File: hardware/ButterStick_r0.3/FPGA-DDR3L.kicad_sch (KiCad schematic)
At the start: 1 part, among them U2 ECP5UM5G_85_CABGA381

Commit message: hw.r0_3: major blocks roughly routed
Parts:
- renumbered U2 to U4
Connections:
- net 1v35: no longer U4.L14 (VCCIO3[3]), U4.L15 (VCCIO3[3]), U4.M15 (VCCIO3[3]), U4.M18 (PR50D/RDQ53), U4.M19 (PR47D/PCLKC3_0/RDQ53), U4.N19 (PR83A/RDQ89), U4.T20 (PR86C/RDQ89), U4.U16 (PR92C/LRC_GPLL0T_IN/RDQ89)
- net A0: no longer U4.U17 (PR92B/RDQ89)
- net A1: now also U4.H18 (PR20A/RDQ17); no longer U4.H20 (PR41B/RDQSN41)
- net A10: now also U4.J18 (PR41C/GR_PCLK2_0/RDQ41); no longer U4.K20 (PR44D/PCLKC2_0/RDQ41)
- net A15: now also U4.J16 (PR20D/RDQ17); no longer U4.K19 (PR44B/PCLKC2_1/RDQ41)
- net A5: no longer U4.T17 (PR92D/LRC_GPLL0C_IN/RDQ89)
- net A7: now also U4.H17 (PR20B/RDQ17); no longer U4.J19 (PR44A/PCLKT2_1/RDQ41)
- net BA1: no longer U4.M20 (PR47B/PCLKC3_1/RDQ53)
- net CK1_N: now also U4.K19 (PR44B/PCLKC2_1/RDQ41)
- net CK1_P: now also U4.J19 (PR44A/PCLKT2_1/RDQ41)
- net CKE1: now also U4.K20 (PR44D/PCLKC2_0/RDQ41); no longer U4.J16 (PR20D/RDQ17)
- net CS1: now also U4.H20 (PR41B/RDQSN41); no longer U4.H16 (PR17D/RDQ17)
- net DQ0: no longer U4.U19 (PR89C/RDQ89)
- net DQ1: no longer U4.T18 (PR89D/RDQ89)
- net DQ10: no longer U4.L16 (PR50A/GR_PCLK3_0/RDQ53)
- net DQ11: no longer U4.R16 (PR56C/RDQ53)
- net DQ12: no longer U4.N18 (PR53C/RDQ53)
- net DQ13: no longer U4.R17 (PR56D/RDQ53)
- net DQ14: no longer U4.N17 (PR56A/RDQ53)
- net DQ15: no longer U4.P17 (PR53D/RDQ53)
- net DQ2: no longer U4.U18 (PR92A/RDQ89)
- net DQ3: no longer U4.R20 (PR86B/RDQ89)
- net DQ4: no longer U4.P18 (PR83D/RDQ89)
- net DQ5: no longer U4.P20 (PR86A/RDQ89)
- net DQ6: no longer U4.P19 (PR83C/RDQ89)
- net DQ7: no longer U4.N20 (PR83B/RDQ89)
- net DQ8: no longer U4.L19 (PR47C/PCLKT3_0/RDQ53)
- net DQ9: no longer U4.L17 (PR50B/RDQ53)
- net LDM: no longer U4.U20 (PR86D/RDQ89)
- net LDQS_N: no longer U4.R18 (PR89B/RDQSN89)
- net LDQS_P: no longer U4.T19 (PR89A/RDQS89)
- net UDM: no longer U4.L18 (PR50C/GR_PCLK3_1/RDQ53)
- net UDQS_N: no longer U4.M17 (PR53B/RDQSN53)
- net UDQS_P: no longer U4.N16 (PR53A/RDQS53)
- net VREF: no longer U4.P16 (PR56B/VREF1_3/RDQ53)
- new net: U4.L14 (VCCIO3[3]), U4.L15 (VCCIO3[3]), U4.M15 (VCCIO3[3])
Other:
- moved on the sheet: U4E
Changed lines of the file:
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@@
   (page 8 19)
   (paper "A4")
-  (no_connect (at 90.17 97.79))
   (no_connect (at 176.53 95.25))
   (no_connect (at 90.17 95.25))
-  (wire (pts (xy 59.69 80.01) (xy 78.74 80.01)))
-  (wire (pts (xy 66.04 95.25) (xy 73.66 95.25)))
-  (wire (pts (xy 66.04 97.79) (xy 73.66 97.79)))
+  (no_connect (at 90.17 97.79))
+  (wire (pts (xy 59.69 124.46) (xy 78.74 124.46)))
   (wire (pts (xy 82.55 54.61) (xy 90.17 54.61)))
   (wire (pts (xy 82.55 57.15) (xy 90.17 57.15)))
@@
   (wire (pts (xy 82.55 74.93) (xy 90.17 74.93)))
   (wire (pts (xy 82.55 77.47) (xy 90.17 77.47)))
-  (wire (pts (xy 82.55 82.55) (xy 90.17 82.55)))
+  (wire (pts (xy 82.55 85.09) (xy 90.17 85.09)))
+  (wire (pts (xy 82.55 87.63) (xy 90.17 87.63)))
   (wire (pts (xy 82.55 90.17) (xy 90.17 90.17)))
   (wire (pts (xy 82.55 92.71) (xy 90.17 92.71)))
@@
   (wire (pts (xy 82.55 120.65) (xy 90.17 120.65)))
   (wire (pts (xy 82.55 123.19) (xy 90.17 123.19)))
+  (wire (pts (xy 82.55 125.73) (xy 90.17 125.73)))
   (wire (pts (xy 82.55 128.27) (xy 90.17 128.27)))
   (wire (pts (xy 82.55 130.81) (xy 90.17 130.81)))
@@
     (effects (font (size 0.508 0.508)) (justify left bottom))
   )
-  (label "A2" (at 59.69 80.01 0)
-    (effects (font (size 1.27 1.27)) (justify left bottom))
-  )
-  (label "CK1_P" (at 66.04 95.25 0)
-    (effects (font (size 1.27 1.27)) (justify left bottom))
-  )
-  (label "CK1_N" (at 66.04 97.79 0)
+  (label "A2" (at 59.69 124.46 0)
     (effects (font (size 1.27 1.27)) (justify left bottom))
   )
@@
     (effects (font (size 1.27 1.27)) (justify left bottom))
   )
-  (label "CS1" (at 82.55 82.55 0)
+  (label "A1" (at 82.55 85.09 0)
+    (effects (font (size 1.27 1.27)) (justify left bottom))
+  )
+  (label "A7" (at 82.55 87.63 0)
     (effects (font (size 1.27 1.27)) (justify left bottom))
   )
@@
     (effects (font (size 1.27 1.27)) (justify left bottom))
   )
-  (label "CKE1" (at 82.55 92.71 0)
+  (label "A15" (at 82.55 92.71 0)
     (effects (font (size 1.27 1.27)) (justify left bottom))
   )
@@
     (effects (font (size 1.27 1.27)) (justify left bottom))
   )
-  (label "A1" (at 82.55 123.19 0)
+  (label "CS1" (at 82.55 123.19 0)
+    (effects (font (size 1.27 1.27)) (justify left bottom))
+  )
+  (label "A10" (at 82.55 125.73 0)
     (effects (font (size 1.27 1.27)) (justify left bottom))
   )
@@
     (effects (font (size 1.27 1.27)) (justify left bottom))
   )
-  (label "A7" (at 82.55 130.81 0)
-    (effects (font (size 1.27 1.27)) (justify left bottom))
-  )
-  (label "A15" (at 82.55 133.35 0)
+  (label "CK1_P" (at 82.55 130.81 0)
+    (effects (font (size 1.27 1.27)) (justify left bottom))
+  )
+  (label "CK1_N" (at 82.55 133.35 0)
     (effects (font (size 1.27 1.27)) (justify left bottom))
   )
@@
     (effects (font (size 1.27 1.27)) (justify left bottom))
   )
-  (label "A10" (at 82.55 138.43 0)
+  (label "CKE1" (at 82.55 138.43 0)
     (effects (font (size 1.27 1.27)) (justify left bottom))
   )
@@
     (effects (font (size 1.27 1.27)) (justify right))
   )
-  (symbol (lib_id "gkl_lattice:ECP5UM5G_85_CABGA381") (at 176.53 54.61 0) (unit 5)
-    (property "Reference" "U2" (id 0) (at 184.15 46.99 0)
+  (symbol (lib_id "gkl_lattice:ECP5UM5G_85_CABGA381") (at 176.53 54.61 0) (mirror x) (unit 5)
+    (property "Reference" "U4" (id 0) (at 184.15 62.23 0)
       (effects (font (size 1.524 1.524)) (justify left))
     )
-    (property "Value" "ECP5UM5G_85_CABGA381" (id 1) (at 182.88 49.53 0)
+    (property "Value" "ECP5UM5G_85_CABGA381" (id 1) (at 182.88 59.69 0)
       (effects (font (size 1.524 1.524)) (justify left))
     )
-    (property "Footprint" "gkl_housings_bga:caBGA_381_17x17" (id 2) (at 180.34 53.34 0)
+    (property "Footprint" "gkl_housings_bga:caBGA_381_17x17" (id 2) (at 180.34 55.88 0)
       (effects (font (size 1.524 1.524)) (justify right) hide)
     )
-    (property "Datasheet" "" (id 3) (at 180.34 58.42 0)
+    (property "Datasheet" "" (id 3) (at 180.34 50.8 0)
       (effects (font (size 1.524 1.524)) (justify right) hide)
     )
-    (property "manf#" "ECP5UM5G_85" (id 4) (at 180.34 55.88 0)
+    (property "manf#" "ECP5UM5G_85" (id 4) (at 180.34 53.34 0)
       (effects (font (size 1.524 1.524)) (justify right) hide)
     )
   )
   (symbol (lib_id "gkl_lattice:ECP5UM5G_85_CABGA381") (at 90.17 54.61 0) (unit 4)
-    (property "Reference" "U2" (id 0) (at 96.52 46.99 0)
+    (property "Reference" "U4" (id 0) (at 96.52 46.99 0)
       (effects (font (size 1.524 1.524)) (justify left))
     )

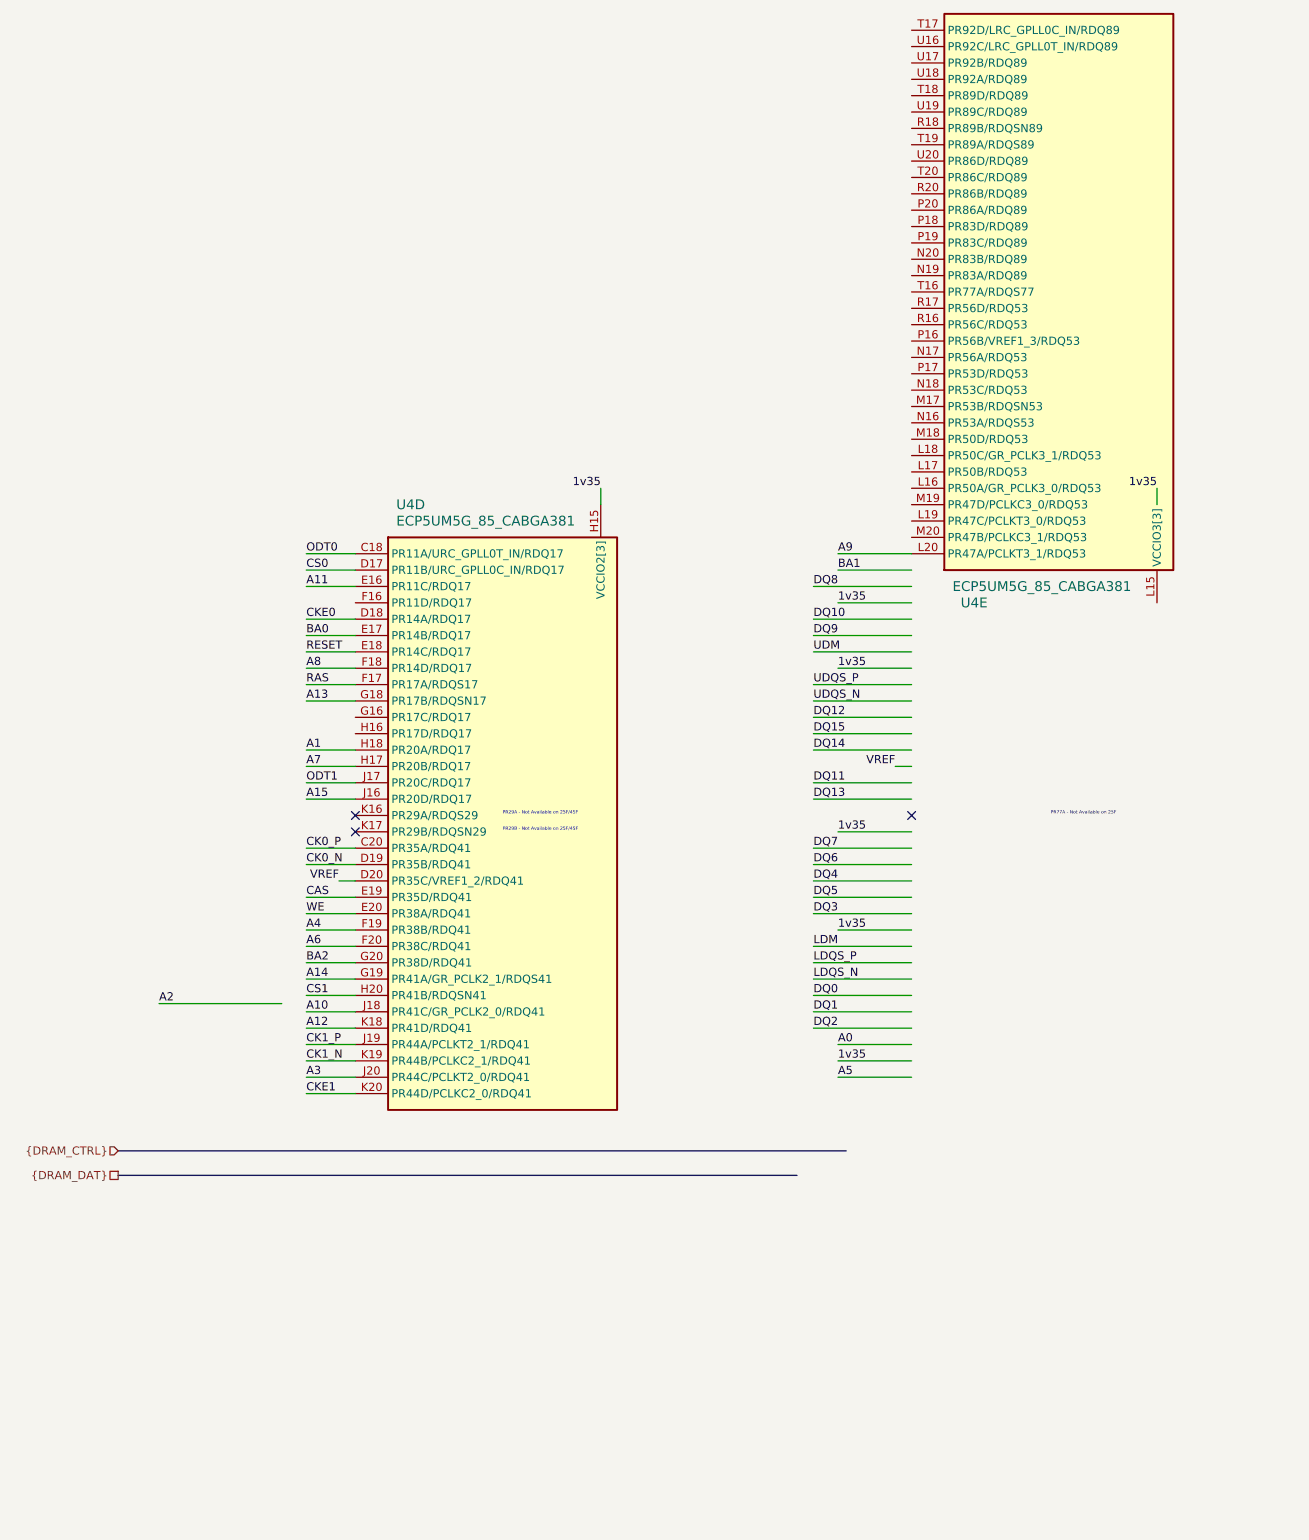
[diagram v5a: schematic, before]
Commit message: hw.r0d3: Length matched all SYZYGY ports
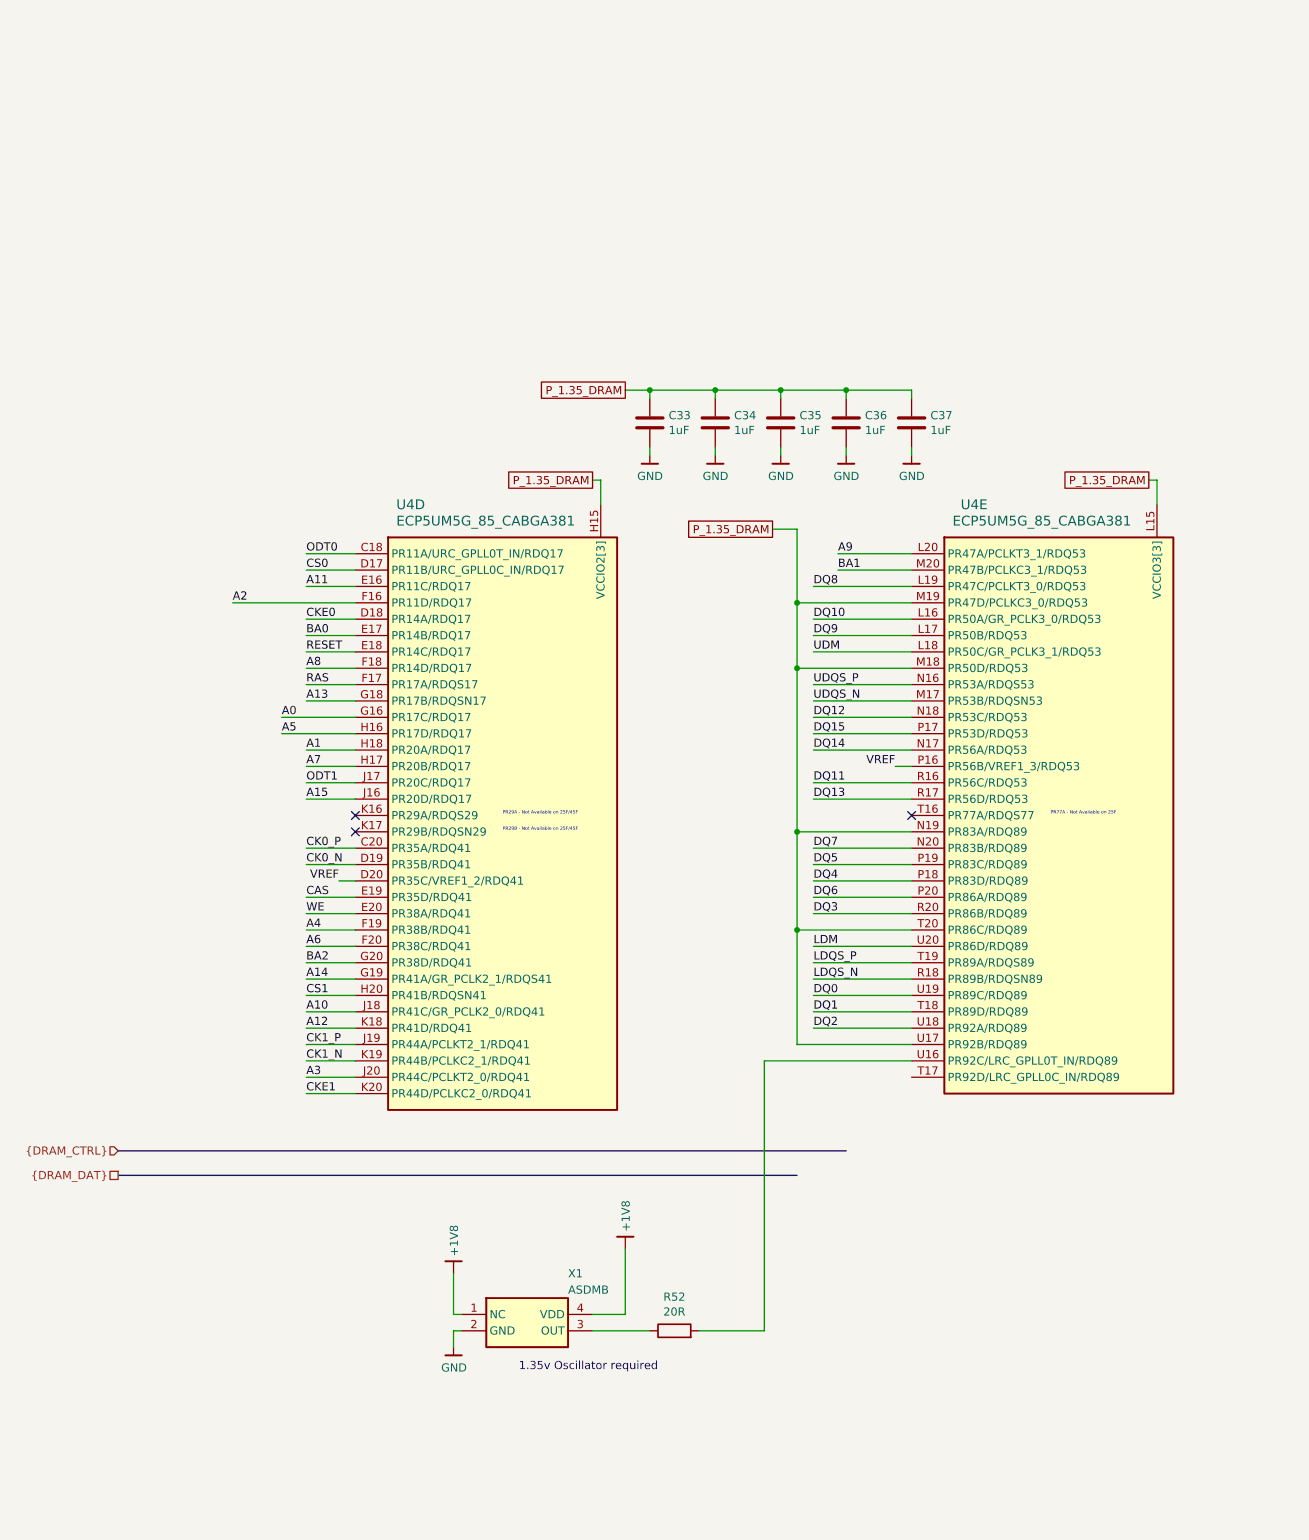
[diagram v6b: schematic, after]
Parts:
- added C33, C34, C35, C36, C37: 1uF, Capacitor_SMD:C_0402_1005Metric, symbol Device:C
- added R52: 20R, Resistor_SMD:R_0402_1005Metric, symbol Device:R
- added X1: ASDMB, gkl_time:Oscilator_2.5x2.0, symbol gkl_time:TYETBCSANF-32.000000
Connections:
- net 1v35 is gone; now on net P_1.35_DRAM: U4.H14 (VCCIO2[3]), U4.H15 (VCCIO2[3]), U4.J15 (VCCIO2[3])
- net A0: now also U4.G16 (PR17C/RDQ17)
- net A2: now also U4.F16 (PR11D/RDQ17)
- net A5: now also U4.H16 (PR17D/RDQ17)
- net BA1: now also U4.M20 (PR47B/PCLKC3_1/RDQ53)
- net DQ0: now also U4.U19 (PR89C/RDQ89)
- net DQ1: now also U4.T18 (PR89D/RDQ89)
- net DQ10: now also U4.L16 (PR50A/GR_PCLK3_0/RDQ53)
- net DQ11: now also U4.R16 (PR56C/RDQ53)
- net DQ12: now also U4.N18 (PR53C/RDQ53)
- net DQ13: now also U4.R17 (PR56D/RDQ53)
- net DQ14: now also U4.N17 (PR56A/RDQ53)
- net DQ15: now also U4.P17 (PR53D/RDQ53)
- net DQ2: now also U4.U18 (PR92A/RDQ89)
- net DQ3: now also U4.R20 (PR86B/RDQ89)
- net DQ4: now also U4.P18 (PR83D/RDQ89)
- net DQ5: now also U4.P19 (PR83C/RDQ89)
- net DQ6: now also U4.P20 (PR86A/RDQ89)
- net DQ7: now also U4.N20 (PR83B/RDQ89)
- net DQ8: now also U4.L19 (PR47C/PCLKT3_0/RDQ53)
- net DQ9: now also U4.L17 (PR50B/RDQ53)
- net LDM: now also U4.U20 (PR86D/RDQ89)
- net LDQS_N: now also U4.R18 (PR89B/RDQSN89)
- net LDQS_P: now also U4.T19 (PR89A/RDQS89)
- net UDM: now also U4.L18 (PR50C/GR_PCLK3_1/RDQ53)
- net UDQS_N: now also U4.M17 (PR53B/RDQSN53)
- net UDQS_P: now also U4.N16 (PR53A/RDQS53)
- net VREF: now also U4.P16 (PR56B/VREF1_3/RDQ53)
- net P_1.35_DRAM: now reaches U4.L14 (VCCIO3[3]), U4.L15 (VCCIO3[3]), U4.M15 (VCCIO3[3])
- net P_1.35_DRAM: now also U4.M18 (PR50D/RDQ53), U4.M19 (PR47D/PCLKC3_0/RDQ53), U4.N19 (PR83A/RDQ89), U4.T20 (PR86C/RDQ89), U4.U17 (PR92B/RDQ89), C33.1, C34.1, C35.1, C36.1, C37.1
- net at U4.U16 (PR92C/LRC_GPLL0T_IN/RDQ89): now also R52.2
- new net: R52.1, X1.3 (OUT)
- new net +1V8: X1.1 (NC), X1.4 (VDD)
- new net GND: C33.2, C34.2, C35.2, C36.2, C37.2, X1.2 (GND)
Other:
- note added: "1.35v Oscillator required"
- moved on the sheet: U4E
